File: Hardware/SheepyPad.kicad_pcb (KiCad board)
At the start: 2 copper layers, 127.6 x 99.7 mm, 60 parts, among them SW1 SW_Push, SW2 Rotary_Encoder_Switch, U1 Sparkfun_Pro_Micro

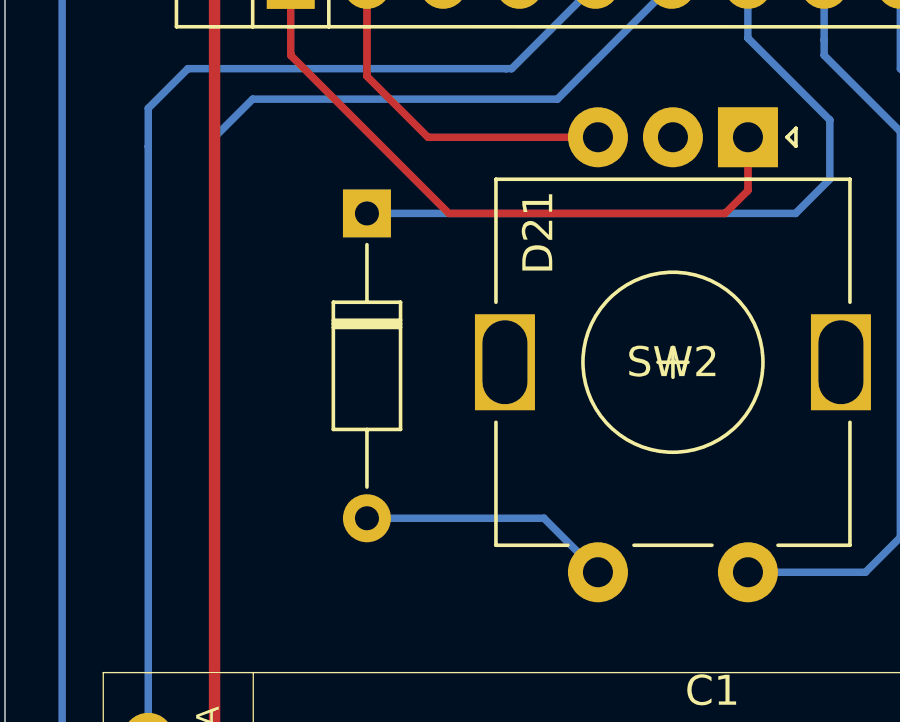
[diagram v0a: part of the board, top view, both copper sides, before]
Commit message: Fixed Diode orientation for encoder SW
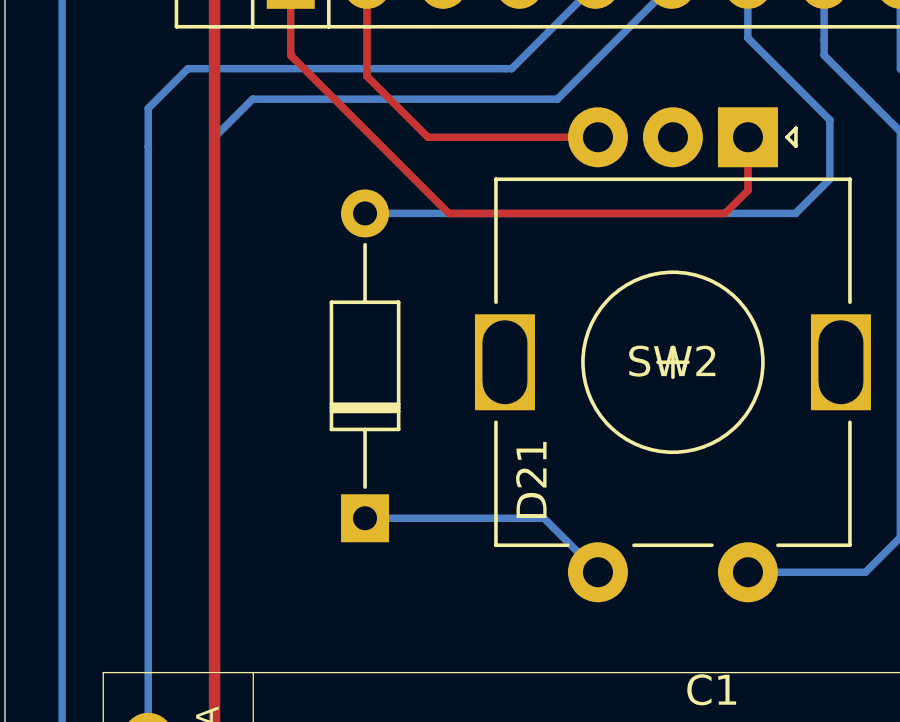
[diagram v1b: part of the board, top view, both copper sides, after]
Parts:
- moved D21 10.2 mm to (69.2, 80.0), turned to 90 degrees
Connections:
- D21 pad 1: /COL_ENC_1 -> Net-(D21-Pad1)
- D21 pad 2: Net-(D21-Pad2) -> /COL_ENC_1
- SW2 pad S1: Net-(D21-Pad2) -> Net-(D21-Pad1)
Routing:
- net Net-(D21-Pad2): track 8.74 -> 0.00 mm
- net Net-(D21-Pad1): track 0.00 -> 8.74 mm
